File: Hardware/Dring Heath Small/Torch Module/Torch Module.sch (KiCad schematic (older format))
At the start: 75 parts, among them J1 Torch, J10 Module conn, J11 Conn_01x18_Male, J12 Conn_01x02_Male, J14 Conn_01x02_Male, J15 Module conn, J2 Module3, J3 Conn_01x18_Male, J4 Limit, J6 Motor, J7 Module1, J8 Torch, J9 2.54 pin, K1 G6E, Q1 IRLML2402, Q2 IRLML2402, Q3 IRLML2402, Q4 IRLML2402, Q5 IRLML2402, U1 ULN2002, U2 NCV8114ASN150T1G, U3 ADS1115IDGS

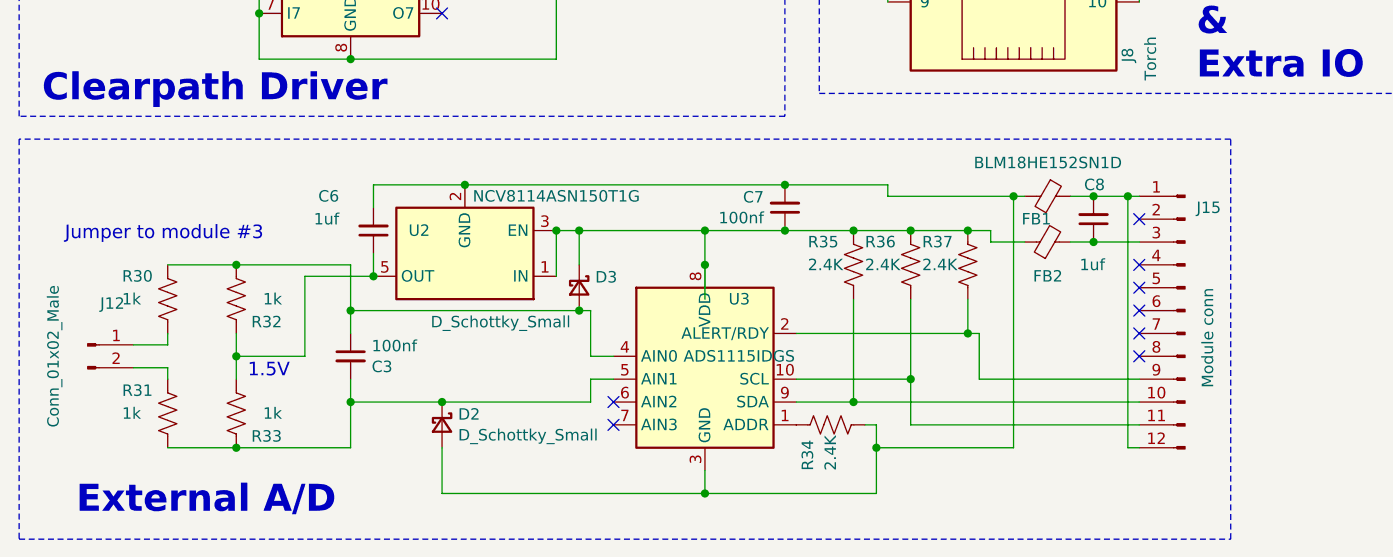
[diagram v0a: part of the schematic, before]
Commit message: Modified clamped A/D input updates panalized boards
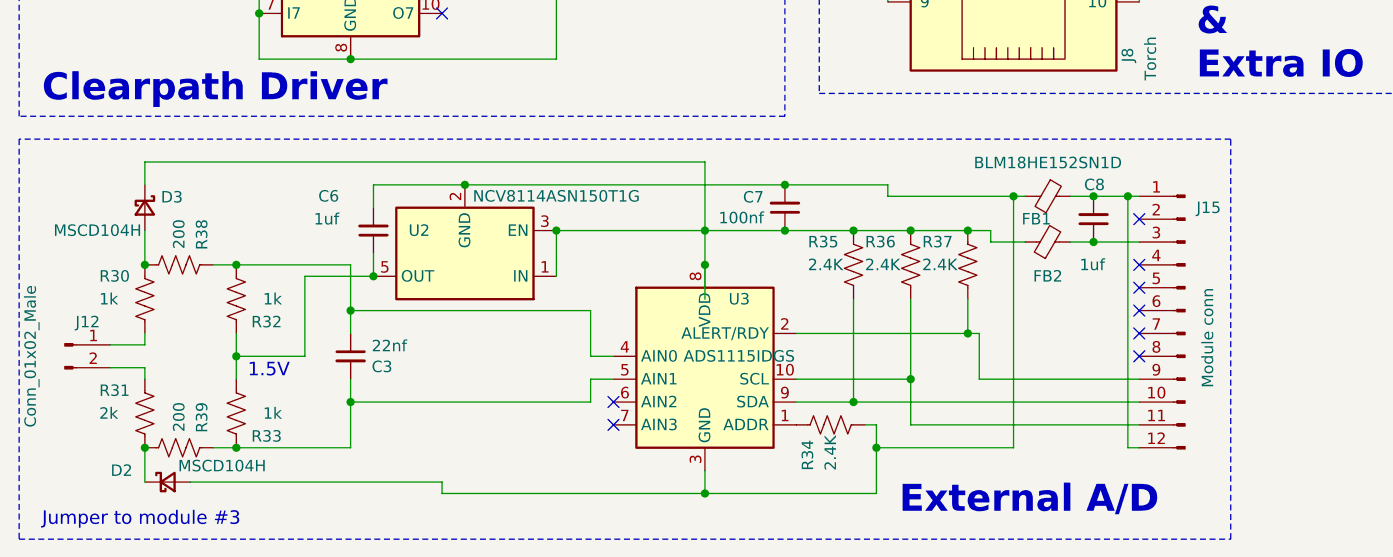
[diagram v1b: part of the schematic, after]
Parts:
- added R38, R39: 200, Resistor_SMD:R_0603_1608Metric_Pad0.98x0.95mm_HandSolder, symbol Device:R_US
- C3: value 100nf -> 22nf
- D2, D3: value D_Schottky_Small -> MSCD104H
- R31: value 1k -> 2k
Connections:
- net at C3.1, R32.2, U3.4 (AIN0): now also R38.1; no longer D3.2 (A), R30.1
- net at C3.2, R33.1, U3.5 (AIN1): now also R39.1; no longer D2.1 (K), R31.2
- new net: D3.2 (A), R30.1, R38.2
- new net: D2.1 (K), R31.2, R39.2
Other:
- moved on the sheet: D2, D3, J12, R30, R31
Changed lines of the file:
@@
 L Connector:Conn_01x02_Male J12
 U 1 1 60319122
-P 1800 5750
-F 0 "J12" H 1908 5931 50  0000 C CNN
-F 1 "Conn_01x02_Male" V 1650 5700 50  0000 C CNN
-F 2 "Connector_PinHeader_2.54mm:PinHeader_1x02_P2.54mm_Vertical" H 1800 5750 50  0001 C CNN
-F 3 "~" H 1800 5750 50  0001 C CNN
-	1    1800 5750
+P 1700 5750
+F 0 "J12" H 1800 5850 50  0000 C CNN
+F 1 "Conn_01x02_Male" V 1550 5700 50  0000 C CNN
+F 2 "Connector_PinHeader_2.54mm:PinHeader_1x02_P2.54mm_Vertical" H 1700 5750 50  0001 C CNN
+F 3 "~" H 1700 5750 50  0001 C CNN
+	1    1700 5750
 	1    0    0    -1
 $EndComp
@@
 L Device:R_US R31
 U 1 1 60367DA6
-P 2150 6050
+P 2050 6050
 AR Path="/60367DA6" Ref="R31"  Part="1"
 AR Path="/61469ABE/60367DA6" Ref="R?"  Part="1"
-F 0 "R31" H 1950 6150 50  0000 L CNN
-F 1 "1k" H 1950 6050 50  0000 L CNN
-F 2 "Resistor_SMD:R_0603_1608Metric_Pad0.98x0.95mm_HandSolder" V 2190 6040 50  0001 C CNN
-F 3 "~" H 2150 6050 50  0001 C CNN
-	1    2150 6050
+F 0 "R31" H 1850 6150 50  0000 L CNN
+F 1 "2k" H 1850 6050 50  0000 L CNN
+F 2 "Resistor_SMD:R_0603_1608Metric_Pad0.98x0.95mm_HandSolder" V 2090 6040 50  0001 C CNN
+F 3 "~" H 2050 6050 50  0001 C CNN
+	1    2050 6050
 	1    0    0    -1
 $EndComp
@@
 L Device:R_US R30
 U 1 1 60368F12
-P 2150 5550
+P 2050 5550
 AR Path="/60368F12" Ref="R30"  Part="1"
 AR Path="/61469ABE/60368F12" Ref="R?"  Part="1"
-F 0 "R30" H 1950 5650 50  0000 L CNN
-F 1 "1k" H 1950 5550 50  0000 L CNN
-F 2 "Resistor_SMD:R_0603_1608Metric_Pad0.98x0.95mm_HandSolder" V 2190 5540 50  0001 C CNN
-F 3 "~" H 2150 5550 50  0001 C CNN
-	1    2150 5550
+F 0 "R30" H 1850 5650 50  0000 L CNN
+F 1 "1k" H 1850 5550 50  0000 L CNN
+F 2 "Resistor_SMD:R_0603_1608Metric_Pad0.98x0.95mm_HandSolder" V 2090 5540 50  0001 C CNN
+F 3 "~" H 2050 5550 50  0001 C CNN
+	1    2050 5550
 	1    0    0    -1
 $EndComp
@@
 AR Path="/61469ABE/6036A3AA" Ref="C?"  Part="1"
 F 0 "C3" H 2858 5754 50  0000 R CNN
-F 1 "100nf" H 2858 5845 50  0000 R CNN
+F 1 "22nf" H 2858 5845 50  0000 R CNN
 F 2 "Capacitor_SMD:C_0603_1608Metric_Pad1.08x0.95mm_HandSolder" H 2950 5800 50  0001 C CNN
 F 3 "~" H 2950 5800 50  0001 C CNN
@@
 Wire Notes Line
 	1500 750  6900 750
-Text Notes 1750 6500 0    118  ~ 24
+Text Notes 5350 6500 0    118  ~ 24
 External A/D
-Text Notes 1700 5300 0    59   ~ 0
+Text Notes 1600 6550 0    59   ~ 0
 Jumper to module #3\n
 Text Notes 3150 950  0    59   ~ 0
@@
 	2450 5700 2450 5800
 Wire Wire Line
-	2000 5850 2150 5850
-Wire Wire Line
-	2150 5850 2150 5900
-Wire Wire Line
-	2000 5750 2150 5750
-Wire Wire Line
-	2150 5750 2150 5700
-Wire Wire Line
-	2150 5400 2450 5400
-Wire Wire Line
-	2150 6200 2450 6200
+	1900 5850 2050 5850
+Wire Wire Line
+	2050 5850 2050 5900
+Wire Wire Line
+	1900 5750 2050 5750
+Wire Wire Line
+	2050 5750 2050 5700
 Wire Wire Line
 	2450 5400 2950 5400
 Wire Wire Line
 	2950 5400 2950 5600
-Connection ~ 2450 5400
 Connection ~ 2950 5600
 Wire Wire Line
@@
 Wire Wire Line
 	2950 6200 2950 6000
-Connection ~ 2450 6200
 Connection ~ 2950 6000
 Wire Wire Line
@@
 Wire Wire Line
 	3850 5450 3850 5250
-Wire Wire Line
-	3850 5250 3950 5250
 Connection ~ 3850 5250
 Connection ~ 4850 5250
@@
 Text Notes 2500 5900 0    59   ~ 0
 1.5V
-Wire Wire Line
-	2950 5600 3950 5600
-Wire Wire Line
-	2950 6000 3350 6000
 $Comp
 L Device:D_Schottky_Small D2
 U 1 1 606DADD6
-P 3350 6100
-F 0 "D2" V 3304 6170 50  0000 L CNN
-F 1 "D_Schottky_Small" V 3395 6170 50  0000 L CNN
-F 2 "Diode_SMD:D_0805_2012Metric_Pad1.15x1.40mm_HandSolder" V 3350 6100 50  0001 C CNN
-F 3 "~" V 3350 6100 50  0001 C CNN
-	1    3350 6100
-	0    1    1    0
-$EndComp
-Connection ~ 3350 6000
-Wire Wire Line
-	3350 6000 4000 6000
+P 2150 6350
+F 0 "D2" H 1900 6400 50  0000 L CNN
+F 1 "MSCD104H" H 2195 6420 50  0000 L CNN
+F 2 "Diode_SMD:D_0805_2012Metric_Pad1.15x1.40mm_HandSolder" V 2150 6350 50  0001 C CNN
+F 3 "~" V 2150 6350 50  0001 C CNN
+	1    2150 6350
+	1    0    0    -1
+$EndComp
 $Comp
 L Device:D_Schottky_Small D3
 U 1 1 606DB922
-P 3950 5500
-F 0 "D3" V 3904 5570 50  0000 L CNN
-F 1 "D_Schottky_Small" V 4100 4850 50  0000 L CNN
-F 2 "Diode_SMD:D_0805_2012Metric_Pad1.15x1.40mm_HandSolder" V 3950 5500 50  0001 C CNN
-F 3 "~" V 3950 5500 50  0001 C CNN
-	1    3950 5500
+P 2050 5150
+F 0 "D3" V 2004 5220 50  0000 L CNN
+F 1 "MSCD104H" V 2150 4750 50  0000 L CNN
+F 2 "Diode_SMD:D_0805_2012Metric_Pad1.15x1.40mm_HandSolder" V 2050 5150 50  0001 C CNN
+F 3 "~" V 2050 5150 50  0001 C CNN
+	1    2050 5150
 	0    1    1    0
 $EndComp
-Connection ~ 3950 5600
-Wire Wire Line
-	3950 5600 4000 5600
-Wire Wire Line
-	3950 5400 3950 5250
-Connection ~ 3950 5250
-Wire Wire Line
-	3950 5250 4500 5250
-Wire Wire Line
-	3350 6200 3350 6400
 Wire Wire Line
 	6350 5100 6350 6200
@@
 	0    1    -1   0
 $EndComp
+$Comp
+L Device:R_US R38
+U 1 1 602730EC
+P 2200 5400
+AR Path="/602730EC" Ref="R38"  Part="1"
+AR Path="/61469ABE/602730EC" Ref="R?"  Part="1"
+F 0 "R38" H 2000 5500 50  0000 L CNN
+F 1 "200" H 2000 5400 50  0000 L CNN
+F 2 "Resistor_SMD:R_0603_1608Metric_Pad0.98x0.95mm_HandSolder" V 2240 5390 50  0001 C CNN
+F 3 "~" H 2200 5400 50  0001 C CNN
+	1    2200 5400
+	0    1    1    0
+$EndComp
+Wire Wire Line
+	2350 5400 2450 5400
+Connection ~ 2450 5400
+Wire Wire Line
+	2050 5400 2050 5250
+Wire Wire Line
+	2950 5600 4000 5600
+Connection ~ 2050 5400
+Wire Wire Line
+	2050 5050 2050 4950
+Wire Wire Line
+	2050 4950 4500 4950
+Wire Wire Line
+	4500 4950 4500 5250
+Wire Wire Line
+	3850 5250 4500 5250
+$Comp
+L Device:R_US R39
+U 1 1 602F56C7
+P 2200 6200
+AR Path="/602F56C7" Ref="R39"  Part="1"
+AR Path="/61469ABE/602F56C7" Ref="R?"  Part="1"
+F 0 "R39" H 2000 6300 50  0000 L CNN
+F 1 "200" H 2000 6200 50  0000 L CNN
+F 2 "Resistor_SMD:R_0603_1608Metric_Pad0.98x0.95mm_HandSolder" V 2240 6190 50  0001 C CNN
+F 3 "~" H 2200 6200 50  0001 C CNN
+	1    2200 6200
+	0    1    1    0
+$EndComp
+Wire Wire Line
+	2350 6200 2450 6200
+Connection ~ 2450 6200
+Wire Wire Line
+	2050 6200 2050 6350
+Wire Wire Line
+	2950 6000 4000 6000
+Connection ~ 2050 6200
+Wire Wire Line
+	2250 6350 3350 6350
+Wire Wire Line
+	3350 6350 3350 6400
 $EndSCHEMATC

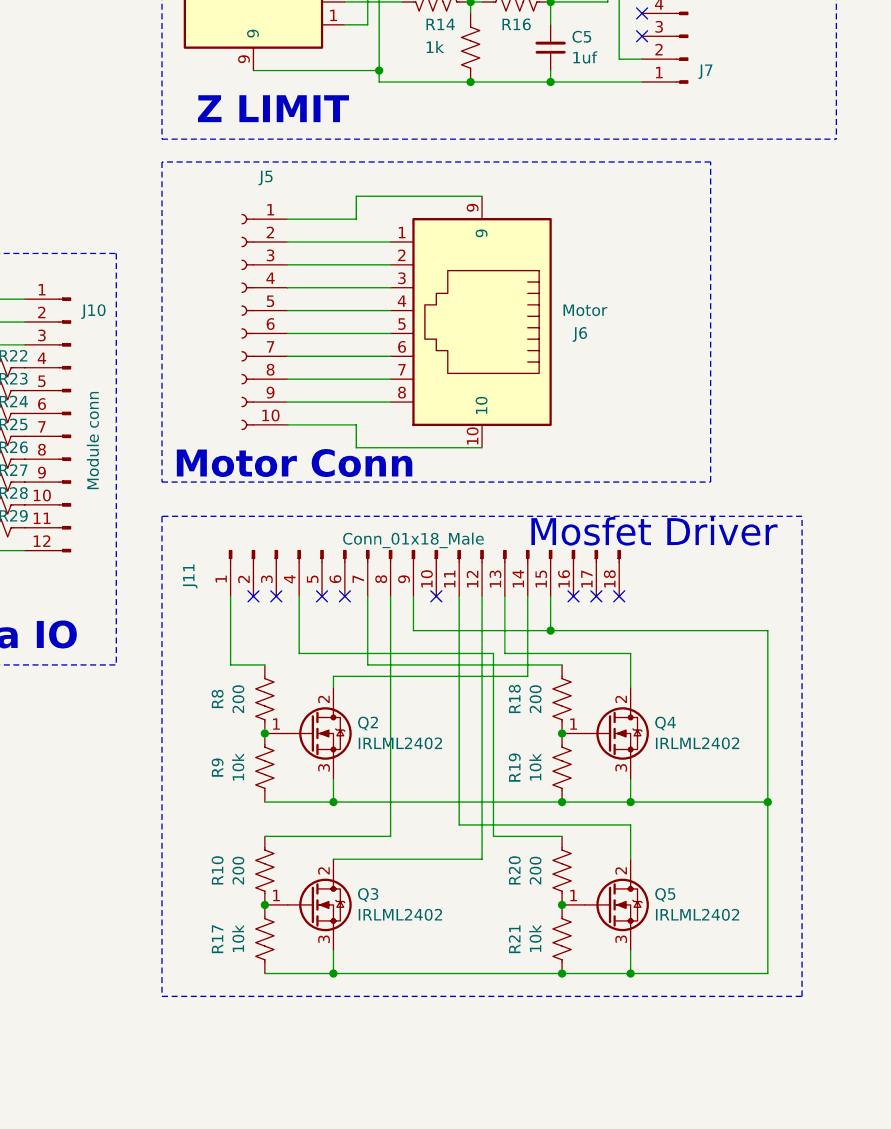
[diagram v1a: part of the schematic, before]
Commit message: Changed RJ45 conector on motor driver module
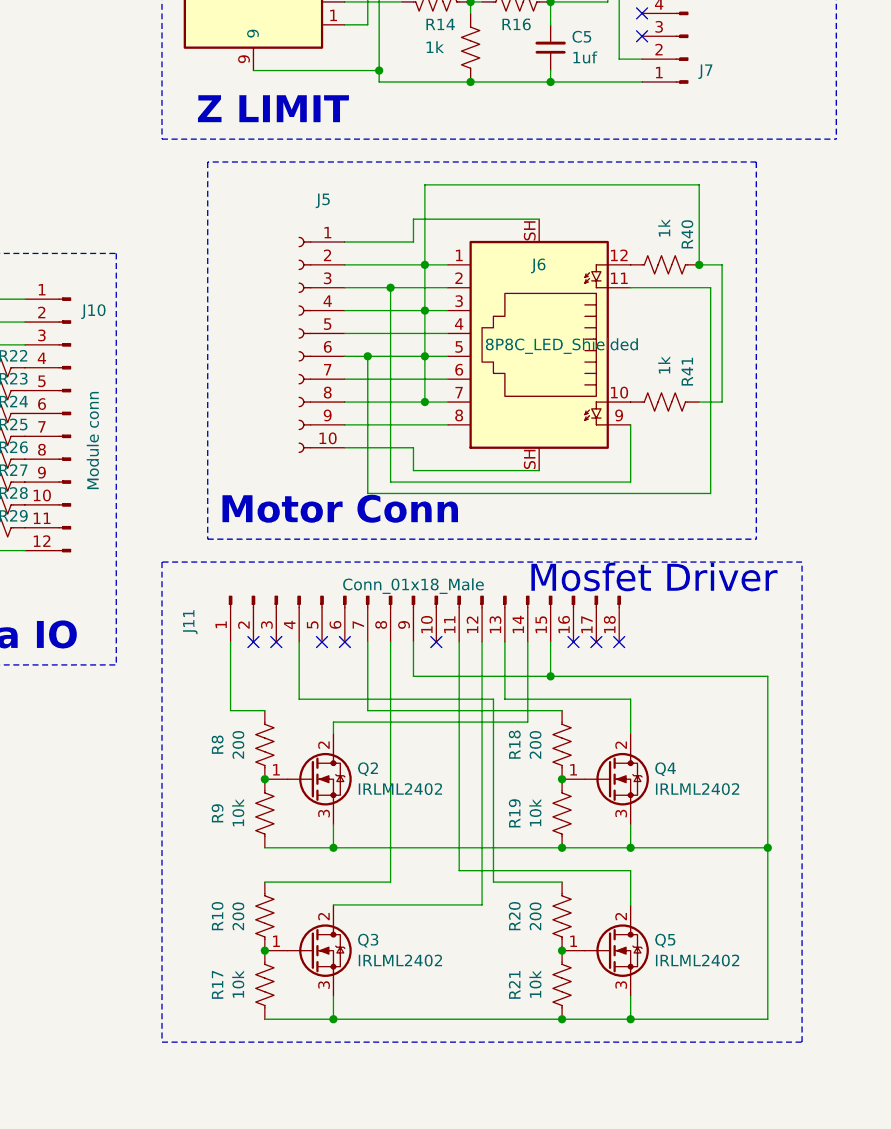
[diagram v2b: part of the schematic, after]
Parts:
- removed J6: Motor, Connector_RJ:RJ45_Amphenol_RJHSE5380, symbol My_library:8P8C_Shielded
- added J6: 8P8C_LED_Shielded, Connector_RJ:RJ45_Amphenol_RJHSE538X, symbol My_library:8P8C_LED_Shielded
- added R40, R41: 1k, Resistor_SMD:R_0603_1608Metric_Pad0.98x0.95mm_HandSolder, symbol Device:R_US
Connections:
- net at J5.1 (Pin_1): now also J6.SH
- net at J5.10 (Pin_10): now also J6.SH
- net at J5.2 (Pin_2): now also J5.4 (Pin_4), J5.6 (Pin_6), J5.8 (Pin_8), J6.1, J6.11, J6.3, J6.5, J6.7, R40.1, R41.1
- net at J5.3 (Pin_3): now also J6.2, J6.9
- net at J5.5 (Pin_5): now also J6.4
- net at J5.7 (Pin_7): now also J6.6
- net at J5.9 (Pin_9): now also J6.8
- new net: J6.10, R41.2
- new net: J6.12, R40.2
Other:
- moved on the sheet: J11, J5, Q2, Q3, Q4, Q5, R10, R17, R18, R19, R20, R21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
